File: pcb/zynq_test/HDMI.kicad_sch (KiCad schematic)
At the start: 66 parts, among them J801 HDMI_A, J802 HDMI_A, J803 Conn_02x04_Odd_Even, U801 ESD8104, U802 ESD8104, U803 TDP1204RNQR, U804 ESD8104, U805 ESD8104, U806 TDP1204RNQR, U807 ESD8104, U808 ESD8104

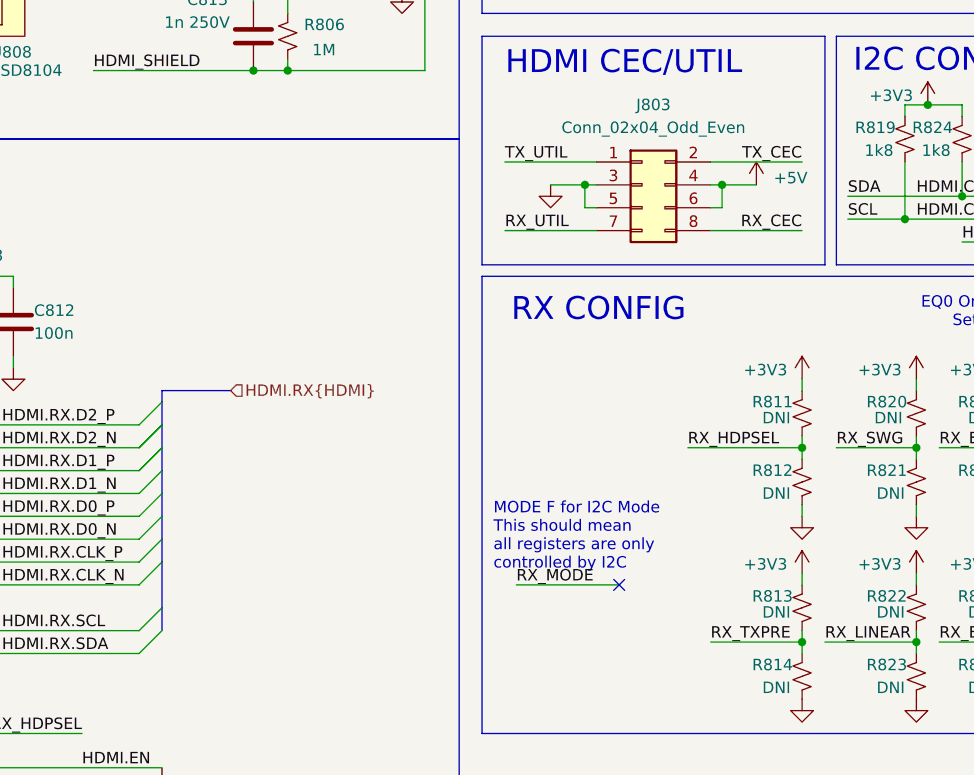
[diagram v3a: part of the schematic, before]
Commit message: Finished most of the schematic, will start routing soon
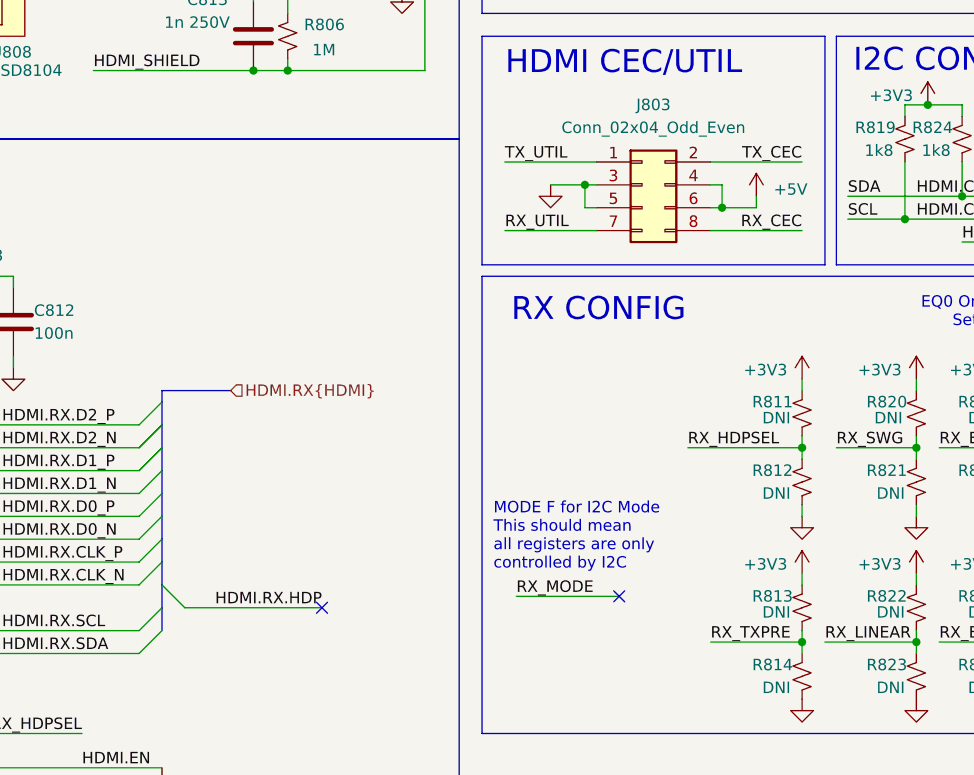
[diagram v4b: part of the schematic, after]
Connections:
- no-connect marks 3 -> 4
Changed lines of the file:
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@@
 	)
 	(junction
+		(at 231.14 106.68)
+		(diameter 0)
+		(color 0 0 0 0)
+	)
+	(junction
 		(at 248.92 68.58)
 		(diameter 0)
@@
 	)
 	(junction
-		(at 231.14 104.14)
-		(diameter 0)
-		(color 0 0 0 0)
-	)
-	(junction
 		(at 111.76 26.67)
 		(diameter 0)
@@
 	)
 	(no_connect
-		(at 219.71 148.59)
+		(at 219.71 149.86)
 	)
 	(no_connect
 		(at 149.86 160.02)
 	)
+	(no_connect
+		(at 186.69 151.13)
+	)
 	(bus_entry
 		(at 168.91 130.81)
@@
 	)
 	(bus_entry
+		(at 168.91 148.59)
+		(size 2.54 2.54)
+		(stroke
+			(width 0)
+			(type default)
+		)
+	)
+	(bus_entry
 		(at 168.91 138.43)
 		(size -2.54 2.54)
@@
 		)
 	)
+	(bus
+		(pts
+			(xy 168.91 148.59) (xy 168.91 151.13)
+		)
+		(stroke
+			(width 0)
+			(type default)
+		)
+	)
 	(wire
 		(pts
@@
 	(wire
 		(pts
-			(xy 219.71 148.59) (xy 208.28 148.59)
+			(xy 219.71 149.86) (xy 208.28 149.86)
 		)
 		(stroke
@@
 	(wire
 		(pts
+			(xy 231.14 104.14) (xy 231.14 106.68)
+		)
+		(stroke
+			(width 0)
+			(type default)
+		)
+	)
+	(wire
+		(pts
 			(xy 106.68 182.88) (xy 95.25 182.88)
 		)
@@
 	(bus
 		(pts
-			(xy 168.91 146.05) (xy 168.91 151.13)
+			(xy 168.91 146.05) (xy 168.91 148.59)
 		)
 		(stroke
@@
 	(wire
 		(pts
-			(xy 231.14 106.68) (xy 231.14 104.14)
-		)
-		(stroke
-			(width 0)
-			(type default)
-		)
-	)
-	(wire
-		(pts
 			(xy 259.08 67.31) (xy 259.08 68.58)
 		)
@@
 	(wire
 		(pts
+			(xy 234.95 106.68) (xy 234.95 105.41)
+		)
+		(stroke
+			(width 0)
+			(type default)
+		)
+	)
+	(wire
+		(pts
 			(xy 274.32 153.67) (xy 274.32 154.94)
 		)
@@
 	(wire
 		(pts
+			(xy 171.45 151.13) (xy 186.69 151.13)
+		)
+		(stroke
+			(width 0)
+			(type default)
+		)
+	)
+	(wire
+		(pts
 			(xy 147.32 90.17) (xy 147.32 91.44)
 		)
@@
 	(wire
 		(pts
-			(xy 231.14 104.14) (xy 234.95 104.14)
+			(xy 231.14 106.68) (xy 234.95 106.68)
 		)
 		(stroke
@@
 		)
 	)
+	(label "HDMI.RX.HDP"
+		(at 186.69 151.13 180)
+		(effects
+			(font
+				(size 1.27 1.27)
+			)
+			(justify right bottom)
+		)
+	)
 	(label "RX_MODE"
-		(at 208.28 148.59 0)
+		(at 208.28 149.86 0)
 		(effects
 			(font
@@
 	(symbol
 		(lib_id "power:+5V")
-		(at 234.95 104.14 0)
+		(at 234.95 105.41 0)
 		(unit 1)
 		(exclude_from_sim no)
@@
 		(dnp no)
 		(property "Reference" "#PWR0824"
-			(at 234.95 107.95 0)
+			(at 234.95 109.22 0)
 			(effects
 				(font
@@
 		)
 		(property "Value" "+5V"
-			(at 238.76 103.378 0)
+			(at 238.76 104.648 0)
 			(effects
 				(font
@@
 		)
 		(property "Footprint" ""
-			(at 234.95 104.14 0)
+			(at 234.95 105.41 0)
 			(effects
 				(font
@@
 		)
 		(property "Datasheet" ""
-			(at 234.95 104.14 0)
+			(at 234.95 105.41 0)
 			(effects
 				(font
@@
 		)
 		(property "Description" "Power symbol creates a global label with name \"+5V\""
-			(at 234.95 104.14 0)
+			(at 234.95 105.41 0)
 			(effects
 				(font

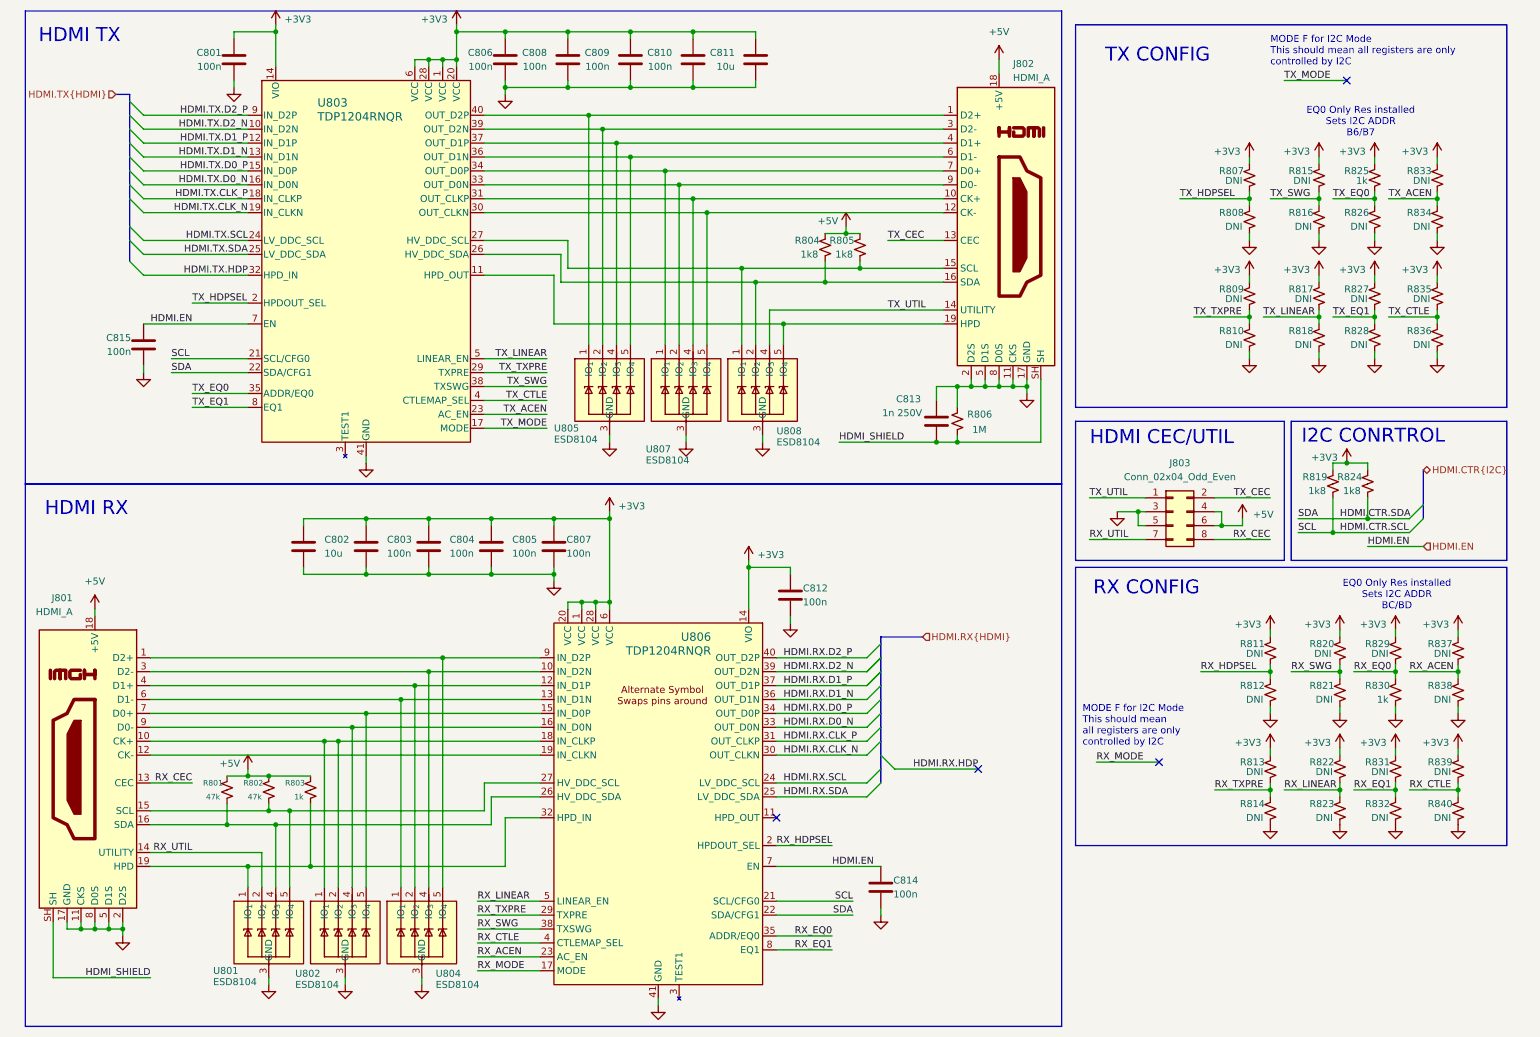
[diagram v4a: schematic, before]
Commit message: finished diff of HDMI
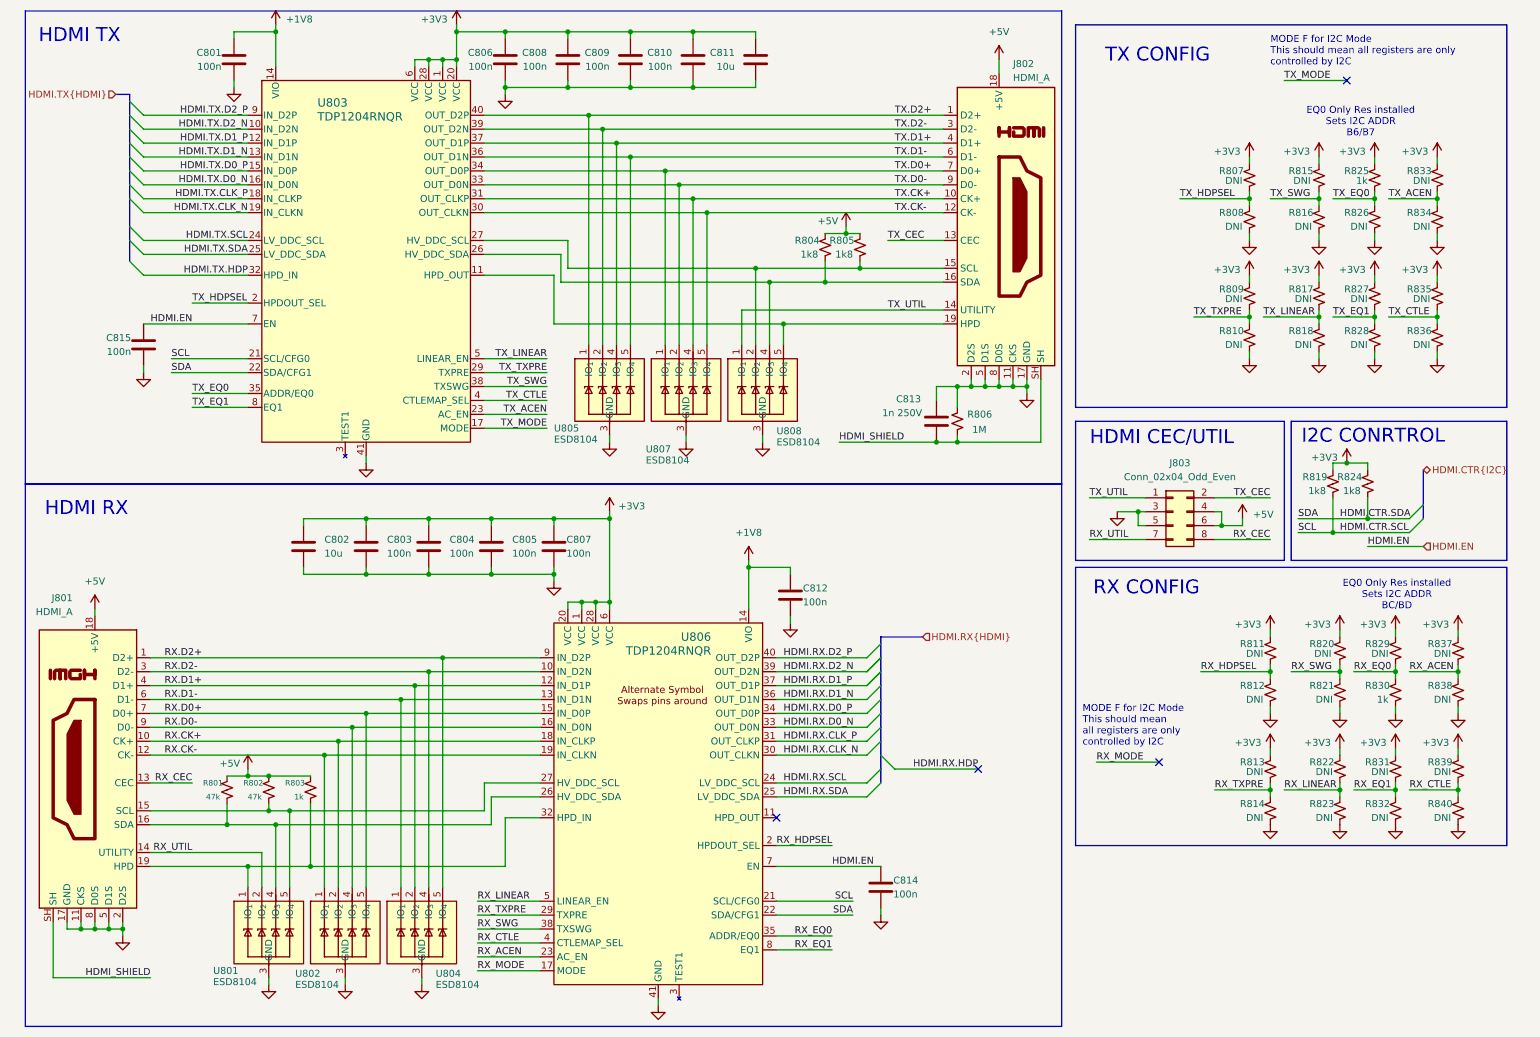
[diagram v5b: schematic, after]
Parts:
- U801, U802, U804, U805, U807, U808: footprint (none) -> Package_DFN_QFN:Diodes_UDFN-10_1.0x2.5mm_P0.5mm
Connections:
- net +3V3: no longer C801.1, C812.1, U803.14 (VIO), U806.14 (VIO)
- net TX_UTIL: now also U808.1 (IO_{1}), U808.10 (N/C); no longer U808.4 (IO_{3}), U808.7 (N/C)
- net RX.D2-: now reaches J801.3 (D2-), U804.4 (IO_{3}), U804.7 (N/C), U806.10 (IN_D2N)
- net RX.D1+: now reaches J801.4 (D1+), U804.2 (IO_{2}), U804.9 (N/C), U806.12 (IN_D1P)
- net RX.D1-: now reaches J801.6 (D1-), U804.1 (IO_{1}), U804.10 (N/C), U806.13 (IN_D1N)
- net RX.D0+: now reaches J801.7 (D0+), U802.5 (IO_{4}), U802.6 (N/C), U806.15 (IN_D0P)
- net RX.D0-: now reaches J801.9 (D0-), U802.4 (IO_{3}), U802.7 (N/C), U806.16 (IN_D0N)
- net RX.CK+: now reaches J801.10 (CK+), U802.2 (IO_{2}), U802.9 (N/C), U806.18 (IN_CLKP)
- net RX.CK+: no longer U802.1 (IO_{1}), U802.10 (N/C)
- net RX.CK-: now reaches J801.12 (CK-), U806.19 (IN_CLKN)
- net RX.CK-: now also U802.1 (IO_{1}), U802.10 (N/C)
- net RX.D2+: now reaches J801.1 (D2+), U804.5 (IO_{4}), U804.6 (N/C), U806.9 (IN_D2P)
- net at J802.15 (SCL), R805.2, U803.27 (HV_DDC_SCL): now also U808.2 (IO_{2}), U808.9 (N/C); no longer U808.1 (IO_{1}), U808.10 (N/C)
- net TX.D0+: now reaches J802.7 (D0+), U803.34 (OUT_D0P), U807.1 (IO_{1}), U807.10 (N/C)
- net TX.D0-: now reaches J802.9 (D0-), U803.33 (OUT_D0N), U807.2 (IO_{2}), U807.9 (N/C)
- net TX.CK+: now reaches J802.10 (CK+), U803.31 (OUT_CLKP), U807.4 (IO_{3}), U807.7 (N/C)
- net TX.CK-: now reaches J802.12 (CK-), U803.30 (OUT_CLKN), U807.5 (IO_{4}), U807.6 (N/C)
- net at J802.16 (SDA), R804.2, U803.26 (HV_DDC_SDA): now also U808.4 (IO_{3}), U808.7 (N/C); no longer U808.2 (IO_{2}), U808.9 (N/C)
- net TX.D1-: now reaches J802.6 (D1-), U803.36 (OUT_D1N), U805.5 (IO_{4}), U805.6 (N/C)
- net TX.D1+: now reaches J802.4 (D1+), U803.37 (OUT_D1P), U805.4 (IO_{3}), U805.7 (N/C)
- net TX.D2-: now reaches J802.3 (D2-), U803.39 (OUT_D2N), U805.2 (IO_{2}), U805.9 (N/C)
- net TX.D2+: now reaches J802.1 (D2+), U803.40 (OUT_D2P), U805.1 (IO_{1}), U805.10 (N/C)
- new net +1V8: C801.1, C812.1, U803.14 (VIO), U806.14 (VIO)

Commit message: Almost done with BOM
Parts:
- added F801: 125mA, Fuse:Fuse_0805_2012Metric, symbol Device:Fuse_Small
- added R841, R842, R843, R844, R845, R846, R847, R848: 49.9R, Resistor_SMD:R_0201_0603Metric, symbol Device:R_Small_US
- C801: renamed from C815; footprint (none) -> Capacitor_SMD:C_0402_1005Metric
- C802: renamed from C801; footprint (none) -> Capacitor_SMD:C_0402_1005Metric
- C803: renamed from C802; footprint (none) -> Capacitor_SMD:C_0805_2012Metric
- C804: renamed from C803; footprint (none) -> Capacitor_SMD:C_0402_1005Metric
- C805: renamed from C804; footprint (none) -> Capacitor_SMD:C_0402_1005Metric
- C806: renamed from C805; footprint (none) -> Capacitor_SMD:C_0402_1005Metric
- C807: renamed from C806; footprint (none) -> Capacitor_SMD:C_0402_1005Metric
- C808: renamed from C807; footprint (none) -> Capacitor_SMD:C_0402_1005Metric
- C809: renamed from C808; footprint (none) -> Capacitor_SMD:C_0402_1005Metric
- C810: renamed from C809; footprint (none) -> Capacitor_SMD:C_0402_1005Metric
- C811: renamed from C810; footprint (none) -> Capacitor_SMD:C_0402_1005Metric
- C812: renamed from C811; footprint (none) -> Capacitor_SMD:C_0805_2012Metric
- C813: renamed from C812; footprint (none) -> Capacitor_SMD:C_0402_1005Metric
- C814: footprint (none) -> Capacitor_SMD:C_0402_1005Metric
- C815: renamed from C813; footprint (none) -> Capacitor_SMD:C_0805_2012Metric
- J803: footprint (none) -> Connector_PinSocket_2.54mm:PinSocket_2x04_P2.54mm_Vertical_SMD
- R801, R802, R803, R804, R805, R819, R824, R825, R830: footprint (none) -> Resistor_SMD:R_0402_1005Metric
- R806: footprint (none) -> Resistor_SMD:R_0805_2012Metric
- R807, R808, R809, R810, R811, R812, R813, R814, R815, R816, R817, R818, R820, R821, R822, R823, R826, R827, R828, R829, R831, R832, R833, R834, R835, R836, R837, R838, R839, R840: footprint (none) -> Resistor_SMD:R_0402_1005Metric; now not fitted
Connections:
- net +1V8 is gone; now on net +3V3: C802.1, C813.1, U803.14 (VIO), U806.14 (VIO)
- net +3V3: now also R841.1, R842.1, R843.1, R844.1, R845.1, R846.1, R847.1, R848.1
- net +5V: now also F801.1; no longer J801.18 (+5V), J802.18 (+5V), R801.1, R802.1, R803.1
- net HDMI.RX.CLK_N: now also R848.2
- net HDMI.RX.CLK_P: now also R847.2
- net HDMI.RX.D0_N: now also R846.2
- net HDMI.RX.D0_P: now also R845.2
- net HDMI.RX.D1_N: now also R844.2
- net HDMI.RX.D1_P: now also R843.2
- net HDMI.RX.D2_N: now also R842.2
- net HDMI.RX.D2_P: now also R841.2
- new net: F801.2, J802.18 (+5V)
- new net +5V_HDMI.RX: J801.18 (+5V), R801.1, R802.1, R803.1

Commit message: Version sent to JLCPCB
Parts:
- C801, C802, C804, C805, C806, C807, C808, C809, C810, C811, C813, C814: JLCPCB Part# (none) -> C1525; PART_NUMBER (none) -> CL05B104KO5NNNC
- C803, C812: JLCPCB Part# (none) -> C15850; PART_NUMBER (none) -> CL21A106KAYNNNE
- C815: JLCPCB Part# (none) -> C440004; PART_NUMBER (none) -> FM21X102K501PXG
- J801, J802: JLCPCB Part# (none) -> C428493; PART_NUMBER (none) -> 10029449-001RLF
- J803: now left out of the parts list
- R801, R802: JLCPCB Part# (none) -> C159985; PART_NUMBER (none) -> RK73H1ETTP4702F
- R803, R825, R830: JLCPCB Part# (none) -> C242161; PART_NUMBER (none) -> ERJ2RKF1001X
- R804, R805, R819, R824: JLCPCB Part# (none) -> C159960; PART_NUMBER (none) -> RK73H1ETTP1801F
- R806: JLCPCB Part# (none) -> C17514; PART_NUMBER (none) -> 0805W8F1004T5E
- R841, R842, R843, R844, R845, R846, R847, R848: JLCPCB Part# (none) -> C170197; PART_NUMBER (none) -> WR02X49R9FAL
- U801, U802, U804, U805, U807, U808: JLCPCB Part# (none) -> C94394; PART_NUMBER (none) -> ESD8104MUTAG
- U803, U806: JLCPCB Part# (none) -> C5216131; PART_NUMBER (none) -> TDP1204RNQR
